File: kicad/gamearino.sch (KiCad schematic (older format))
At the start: 16 parts, among them U1 ESP-12F

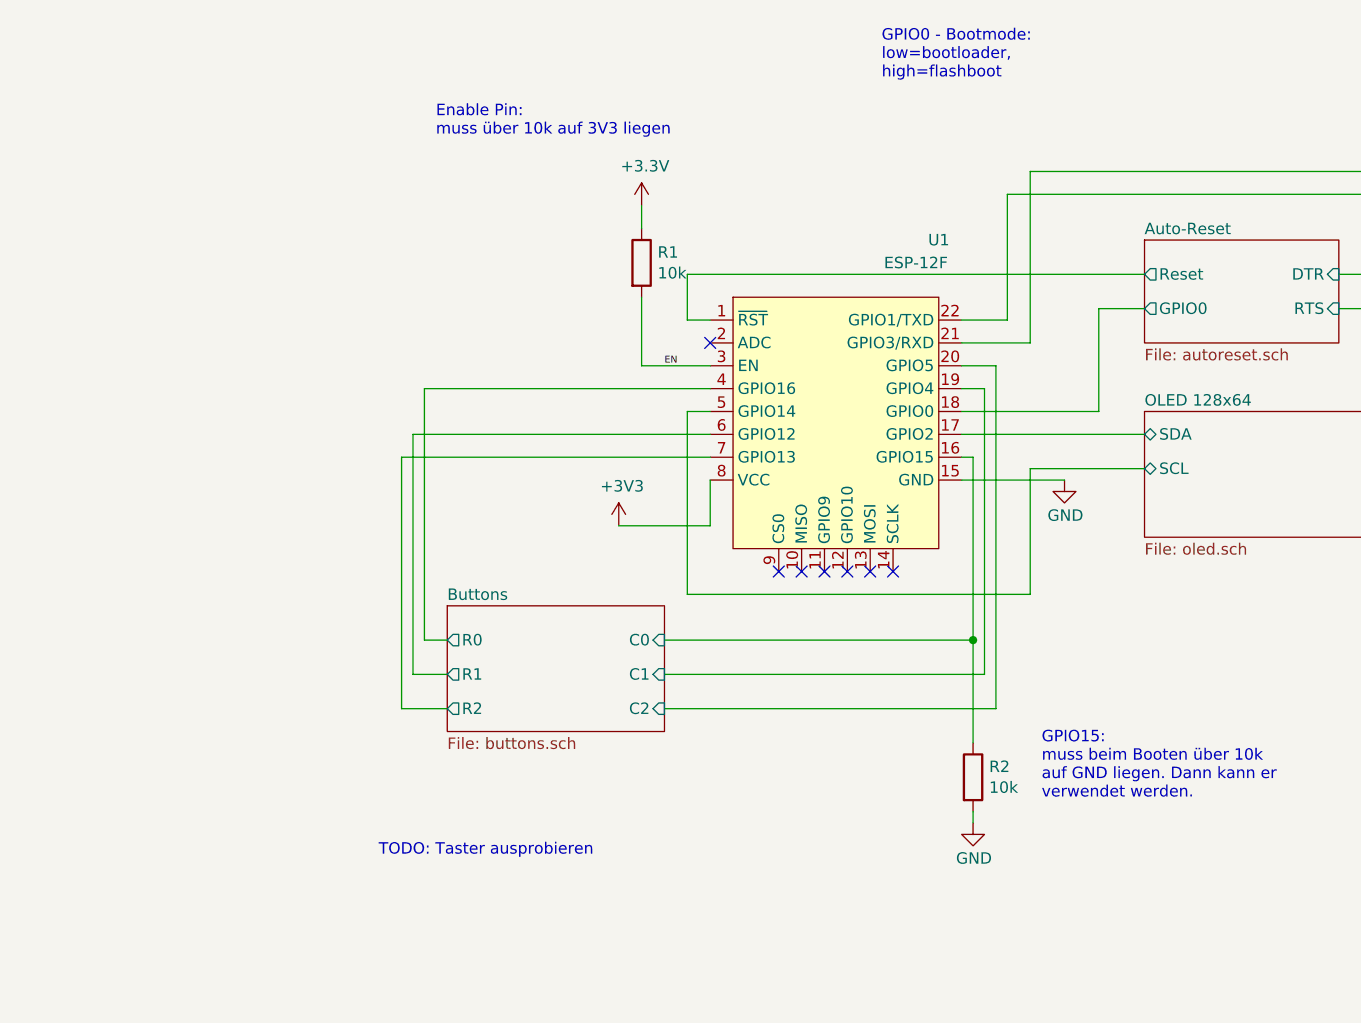
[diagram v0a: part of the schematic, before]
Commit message: Schaltplanänderungen für v20.0.3 eingepflegt
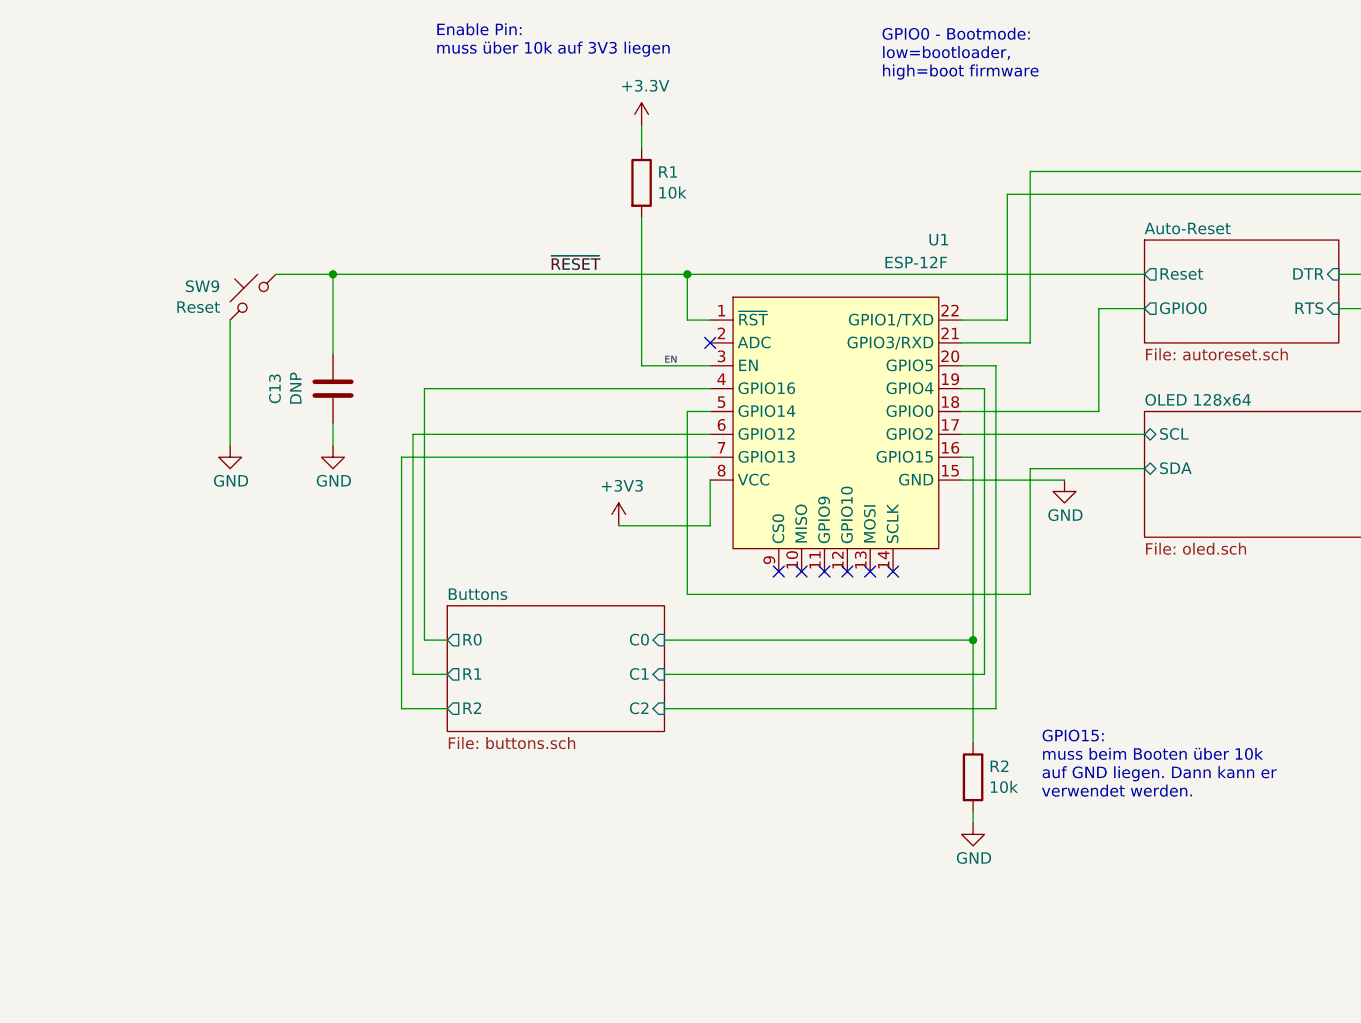
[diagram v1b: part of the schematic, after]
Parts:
- added C13: DNP, Capacitor_SMD:C_0603_1608Metric, symbol Device:C
- added SW9: Reset, htl_smd:SW_Push_5.1mm_H1.5mm, symbol Switch:SW_Push_45deg
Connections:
- net GND: now also C13.2, SW9.1
- net OLED 128x64/SCL: now also U1.17 (GPIO2); no longer U1.5 (GPIO14)
- net OLED 128x64/SDA: now also U1.5 (GPIO14); no longer U1.17 (GPIO2)
- net Auto-Reset/Reset renamed ~RESET
- net ~RESET: now also C13.1, SW9.2
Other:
- note added: "GPIO0 - Bootmode: \nlow=bootloader, \nhigh=boot firmware"
- note removed: "GPIO0 - Bootmode: \nlow=bootloader, \nhigh=flashboot"
- note removed: "TODO: Taster ausprobieren"
- moved on the sheet: R1
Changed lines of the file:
@@
 Sheet 1 5
 Title "Gamearino"
-Date "2021-04-29"
-Rev "V0.0.2"
+Date "2021-05-11"
+Rev "V20.0.3"
 Comp "HTL-Steyr"
 Comment1 "4ABHEL, 2020/2021"
@@
 $EndComp
 Text Notes 5950 2300 0    50   ~ 0
-GPIO0 - Bootmode: \nlow=bootloader, \nhigh=flashboot
+GPIO0 - Bootmode: \nlow=bootloader, \nhigh=boot firmware
 Wire Wire Line
 	6300 3350 6500 3350
@@
 L Device:R R?
 U 1 1 60405618
-P 4900 3100
+P 4900 2750
 AR Path="/603CE165/60405618" Ref="R?"  Part="1"
 AR Path="/60405618" Ref="R1"  Part="1"
-F 0 "R1" H 4970 3146 50  0000 L CNN
-F 1 "10k" H 4970 3055 50  0000 L CNN
-F 2 "Resistor_SMD:R_0603_1608Metric" V 4830 3100 50  0001 C CNN
-F 3 "~" H 4900 3100 50  0001 C CNN
-F 4 "C103210" H 4900 3100 50  0001 C CNN "DistOrderNr"
-F 5 "LCSC" H 4900 3100 50  0001 C CNN "Distributor"
-F 6 "RTT03103JTP" H 4900 3100 50  0001 C CNN "ManPartNr"
-F 7 "RALEC" H 4900 3100 50  0001 C CNN "Manufacturer"
-F 8 "10kΩ ±5% 0.1W ±100ppm/℃" H 4900 3100 50  0001 C CNN "Notes"
-F 9 "0.0015" H 4900 3100 50  0001 C CNN "PriceEUR"
-F 10 "100" H 4900 3100 50  0001 C CNN "PriceForQty"
-	1    4900 3100
+F 0 "R1" H 4970 2796 50  0000 L CNN
+F 1 "10k" H 4970 2705 50  0000 L CNN
+F 2 "Resistor_SMD:R_0603_1608Metric" V 4830 2750 50  0001 C CNN
+F 3 "~" H 4900 2750 50  0001 C CNN
+F 4 "C103210" H 4900 2750 50  0001 C CNN "DistOrderNr"
+F 5 "LCSC" H 4900 2750 50  0001 C CNN "Distributor"
+F 6 "RTT03103JTP" H 4900 2750 50  0001 C CNN "ManPartNr"
+F 7 "RALEC" H 4900 2750 50  0001 C CNN "Manufacturer"
+F 8 "10kΩ ±5% 0.1W ±100ppm/℃" H 4900 2750 50  0001 C CNN "Notes"
+F 9 "0.0015" H 4900 2750 50  0001 C CNN "PriceEUR"
+F 10 "100" H 4900 2750 50  0001 C CNN "PriceForQty"
+	1    4900 2750
 	1    0    0    -1
 $EndComp
@@
 	5200 3550 4900 3550
 Wire Wire Line
-	4900 3550 4900 3250
+	4900 3550 4900 2900
 $Comp
 L power:+3.3V #PWR?
 U 1 1 60406C3E
-P 4900 2850
+P 4900 2500
 AR Path="/5F8674B3/60406C3E" Ref="#PWR?"  Part="1"
 AR Path="/60406C3E" Ref="#PWR02"  Part="1"
 AR Path="/603FCB6F/60406C3E" Ref="#PWR?"  Part="1"
-F 0 "#PWR02" H 4900 2700 50  0001 C CNN
-F 1 "+3.3V" H 4915 3023 50  0000 C CNN
-F 2 "" H 4900 2850 50  0001 C CNN
-F 3 "" H 4900 2850 50  0001 C CNN
-	1    4900 2850
-	1    0    0    -1
-$EndComp
-Wire Wire Line
-	4900 2850 4900 2950
+F 0 "#PWR02" H 4900 2350 50  0001 C CNN
+F 1 "+3.3V" H 4915 2673 50  0000 C CNN
+F 2 "" H 4900 2500 50  0001 C CNN
+F 3 "" H 4900 2500 50  0001 C CNN
+	1    4900 2500
+	1    0    0    -1
+$EndComp
+Wire Wire Line
+	4900 2500 4900 2600
 Wire Wire Line
 	7100 3850 6300 3850
@@
 F0 "OLED 128x64" 50
 F1 "oled.sch" 50
-F2 "SDA" B L 7100 3850 50
-F3 "SCL" B L 7100 4000 50
+F2 "SDA" B L 7100 4000 50
+F3 "SCL" B L 7100 3850 50
 $EndSheet
 $Comp
@@
 	5200 4250 5200 4050
 NoConn ~ 5200 3450
-Text Notes 4000 2550 0    50   ~ 0
+Text Notes 4000 2200 0    50   ~ 0
 Enable Pin:\nmuss über 10k auf 3V3 liegen
 Text Notes 6650 5450 0    50   ~ 0
@@
 NoConn ~ 5900 4450
 NoConn ~ 6000 4450
-Text Notes 3750 5700 0    50   ~ 0
-TODO: Taster ausprobieren
 Text Label 5000 3550 0    30   ~ 0
 EN
@@
 	1    0    0    -1
 $EndComp
+$Comp
+L Device:C C13
+U 1 1 60A4C04A
+P 3550 3650
+F 0 "C13" V 3298 3650 50  0000 C CNN
+F 1 "DNP" V 3389 3650 50  0000 C CNN
+F 2 "Capacitor_SMD:C_0603_1608Metric" H 3588 3500 50  0001 C CNN
+F 3 "~" H 3550 3650 50  0001 C CNN
+	1    3550 3650
+	1    0    0    -1
+$EndComp
+Wire Wire Line
+	3550 3500 3550 3150
+$Comp
+L power:GND #PWR?
+U 1 1 60A4D273
+P 3550 3900
+AR Path="/5F8674B3/60A4D273" Ref="#PWR?"  Part="1"
+AR Path="/60A4D273" Ref="#PWR037"  Part="1"
+F 0 "#PWR037" H 3550 3650 50  0001 C CNN
+F 1 "GND" H 3554 3745 50  0000 C CNN
+F 2 "" H 3550 3900 50  0001 C CNN
+F 3 "" H 3550 3900 50  0001 C CNN
+	1    3550 3900
+	1    0    0    -1
+$EndComp
+Wire Wire Line
+	3550 3900 3550 3800
+$Comp
+L Switch:SW_Push_45deg SW?
+U 1 1 60A50E09
+P 3200 3250
+AR Path="/603CE165/60A50E09" Ref="SW?"  Part="1"
+AR Path="/60A50E09" Ref="SW9"  Part="1"
+F 0 "SW9" V 3246 3393 50  0000 L CNN
+F 1 "Reset" V 3155 3393 50  0000 L CNN
+F 2 "htl_smd:SW_Push_5.1mm_H1.5mm" H 3200 3450 50  0001 C CNN
+F 3 "~" H 3200 3450 50  0001 C CNN
+F 4 "C318884" H 3200 3250 50  0001 C CNN "DistOrderNr"
+F 5 "LCSC" H 3200 3250 50  0001 C CNN "Distributor"
+F 6 "TS-1187A-B-A-B" H 3200 3250 50  0001 C CNN "ManPartNr"
+F 7 "XKB Connectivity" H 3200 3250 50  0001 C CNN "Manufacturer"
+F 8 "SMD Taster h=1.2/1.5mm" H 3200 3250 50  0001 C CNN "Notes"
+F 9 "0.0129" H 3200 3250 50  0001 C CNN "PriceEUR"
+F 10 "50" H 3200 3250 50  0001 C CNN "PriceForQty"
+	1    3200 3250
+	0    -1   -1   0
+$EndComp
+Wire Wire Line
+	3550 3150 5100 3150
+Connection ~ 5100 3150
+Text Label 4500 3150 0    50   ~ 0
+~RESET
+Wire Wire Line
+	3300 3150 3550 3150
+Connection ~ 3550 3150
+$Comp
+L power:GND #PWR?
+U 1 1 60A56409
+P 3100 3900
+AR Path="/5F8674B3/60A56409" Ref="#PWR?"  Part="1"
+AR Path="/60A56409" Ref="#PWR041"  Part="1"
+F 0 "#PWR041" H 3100 3650 50  0001 C CNN
+F 1 "GND" H 3104 3745 50  0000 C CNN
+F 2 "" H 3100 3900 50  0001 C CNN
+F 3 "" H 3100 3900 50  0001 C CNN
+	1    3100 3900
+	1    0    0    -1
+$EndComp
+Wire Wire Line
+	3100 3900 3100 3350
 $EndSCHEMATC

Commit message: Layoutbugfixes, v20.0.3 fertig, CAM-Daten
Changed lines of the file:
@@
 F0 "Auto-Reset" 50
 F1 "autoreset.sch" 50
-F2 "Reset" O L 7100 3150 50
-F3 "GPIO0" O L 7100 3300 50
-F4 "DTR" I R 7950 3150 50
-F5 "RTS" I R 7950 3300 50
+F2 "GPIO0" O L 7100 3300 50
+F3 "DTR" I R 7950 3150 50
+F4 "RTS" I R 7950 3300 50
+F5 "~RESET" O L 7100 3150 50
 $EndSheet
 Wire Wire Line

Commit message: 76 Stk. bei Multi-CB bestellt
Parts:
- Item7: value SMD-Schablone: 120um, Edelstahl, 25mm Umlaufender Überstand, Pastenreduktion 30um im PCB-Design -> SMD-Schablone: 120um, Edelstahl, 35mm Umlaufender Überstand, Pastenreduktion 30um im PCB-Design
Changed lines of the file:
@@
 P 800 7600
 F 0 "Item7" H 930 7646 50  0000 L CNN
-F 1 "SMD-Schablone: 120um, Edelstahl, 25mm Umlaufender Überstand, Pastenreduktion 30um im PCB-Design" H 930 7555 50  0000 L CNN
+F 1 "SMD-Schablone: 120um, Edelstahl, 35mm Umlaufender Überstand, Pastenreduktion 30um im PCB-Design" H 930 7555 50  0000 L CNN
 F 2 "" H 800 7530 50  0001 C CNN
 F 3 "~" V 800 7600 50  0001 C CNN
